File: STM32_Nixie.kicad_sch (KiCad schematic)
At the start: 0 parts

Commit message: added mcu symbol
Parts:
- added U?: STM32F100C4Tx, Package_QFP:LQFP-48_7x7mm_P0.5mm, symbol MCU_ST_STM32F1:STM32F100C4Tx
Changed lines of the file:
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@@
 (kicad_sch (version 20211123) (generator eeschema)
   (paper "A4")
+  (symbol (lib_id "MCU_ST_STM32F1:STM32F100C4Tx") (at 86.36 100.33 0) (unit 1)
+    (in_bom yes) (on_board yes) (fields_autoplaced)
+    (property "Reference" "U?" (id 0) (at 90.9194 138.43 0)
+      (effects (font (size 1.27 1.27)) (justify left))
+    )
+    (property "Value" "STM32F100C4Tx" (id 1) (at 90.9194 140.97 0)
+      (effects (font (size 1.27 1.27)) (justify left))
+    )
+    (property "Footprint" "Package_QFP:LQFP-48_7x7mm_P0.5mm" (id 2) (at 71.12 135.89 0)
+      (effects (font (size 1.27 1.27)) (justify right) hide)
+    )
+    (property "Datasheet" "http://www.st.com/st-web-ui/static/active/en/resource/technical/document/datasheet/CD00251732.pdf" (id 3) (at 86.36 100.33 0)
+      (effects (font (size 1.27 1.27)) hide)
+    )
+    (pin "1")
+    (pin "10")
+    (pin "11")
+    (pin "12")
+    (pin "13")
+    (pin "14")
+    (pin "15")
+    (pin "16")
+    (pin "17")
+    (pin "18")
+    (pin "19")
+    (pin "2")
+    (pin "20")
+    (pin "21")
+    (pin "22")
+    (pin "23")
+    (pin "24")
+    (pin "25")
+    (pin "26")
+    (pin "27")
+    (pin "28")
+    (pin "29")
+    (pin "3")
+    (pin "30")
+    (pin "31")
+    (pin "32")
+    (pin "33")
+    (pin "34")
+    (pin "35")
+    (pin "36")
+    (pin "37")
+    (pin "38")
+    (pin "39")
+    (pin "4")
+    (pin "40")
+    (pin "41")
+    (pin "42")
+    (pin "43")
+    (pin "44")
+    (pin "45")
+    (pin "46")
+    (pin "47")
+    (pin "48")
+    (pin "5")
+    (pin "6")
+    (pin "7")
+    (pin "8")
+    (pin "9")
+  )
   (sheet_instances
     (path "/" (page "1"))
   )
+  (symbol_instances
+    (path "/0270b2c5-4cd0-40ed-86dd-bdd60fed1e2d"
+      (reference "U?") (unit 1) (value "STM32F100C4Tx") (footprint "Package_QFP:LQFP-48_7x7mm_P0.5mm")
+    )
+  )
 )

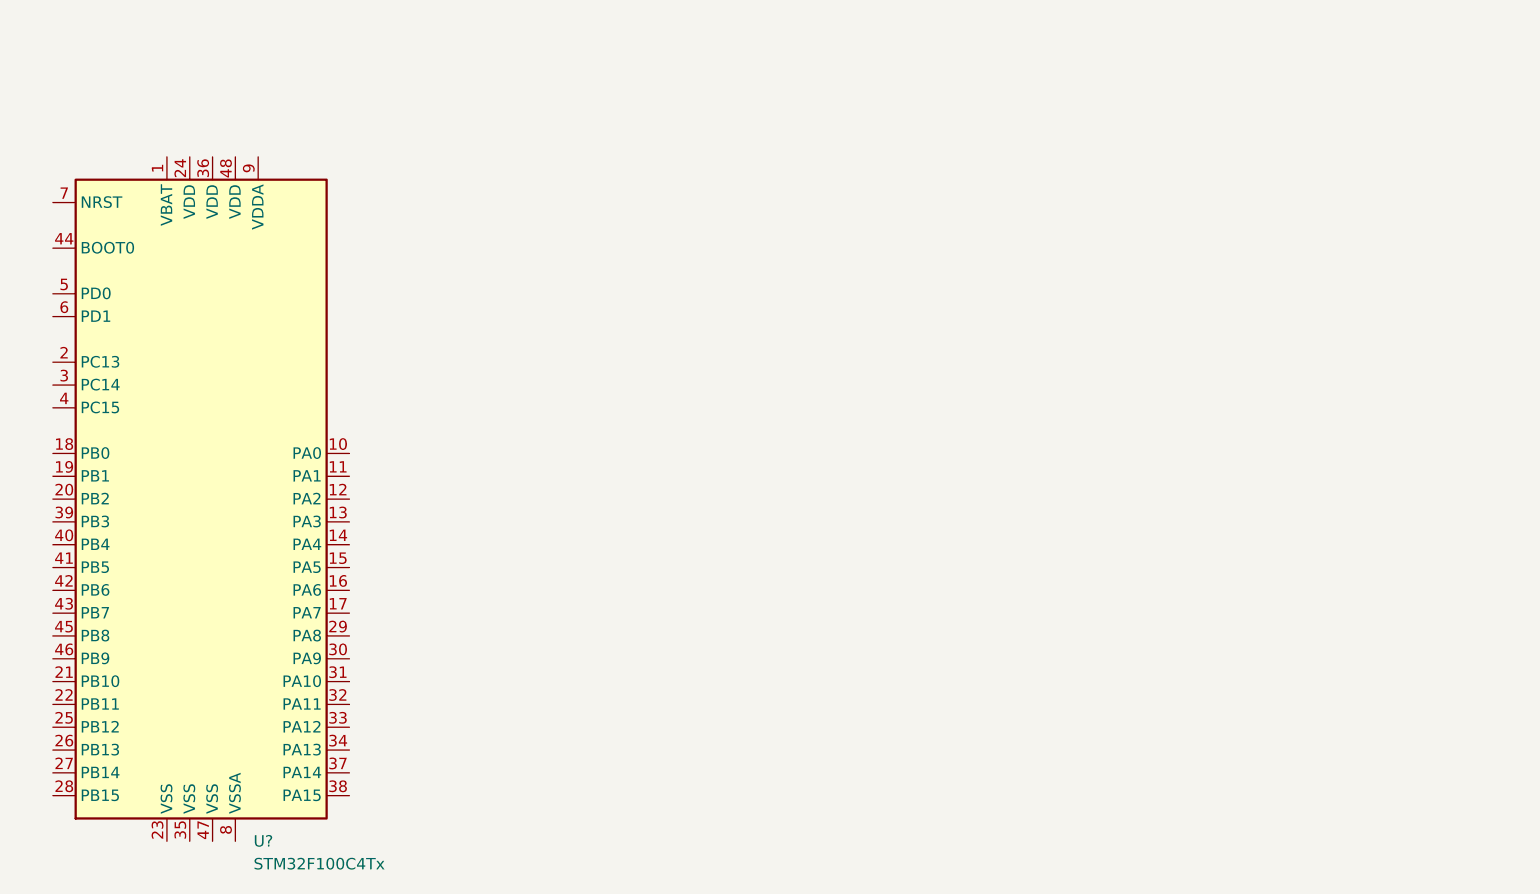
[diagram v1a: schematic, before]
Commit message: Added MCU page and shift register.
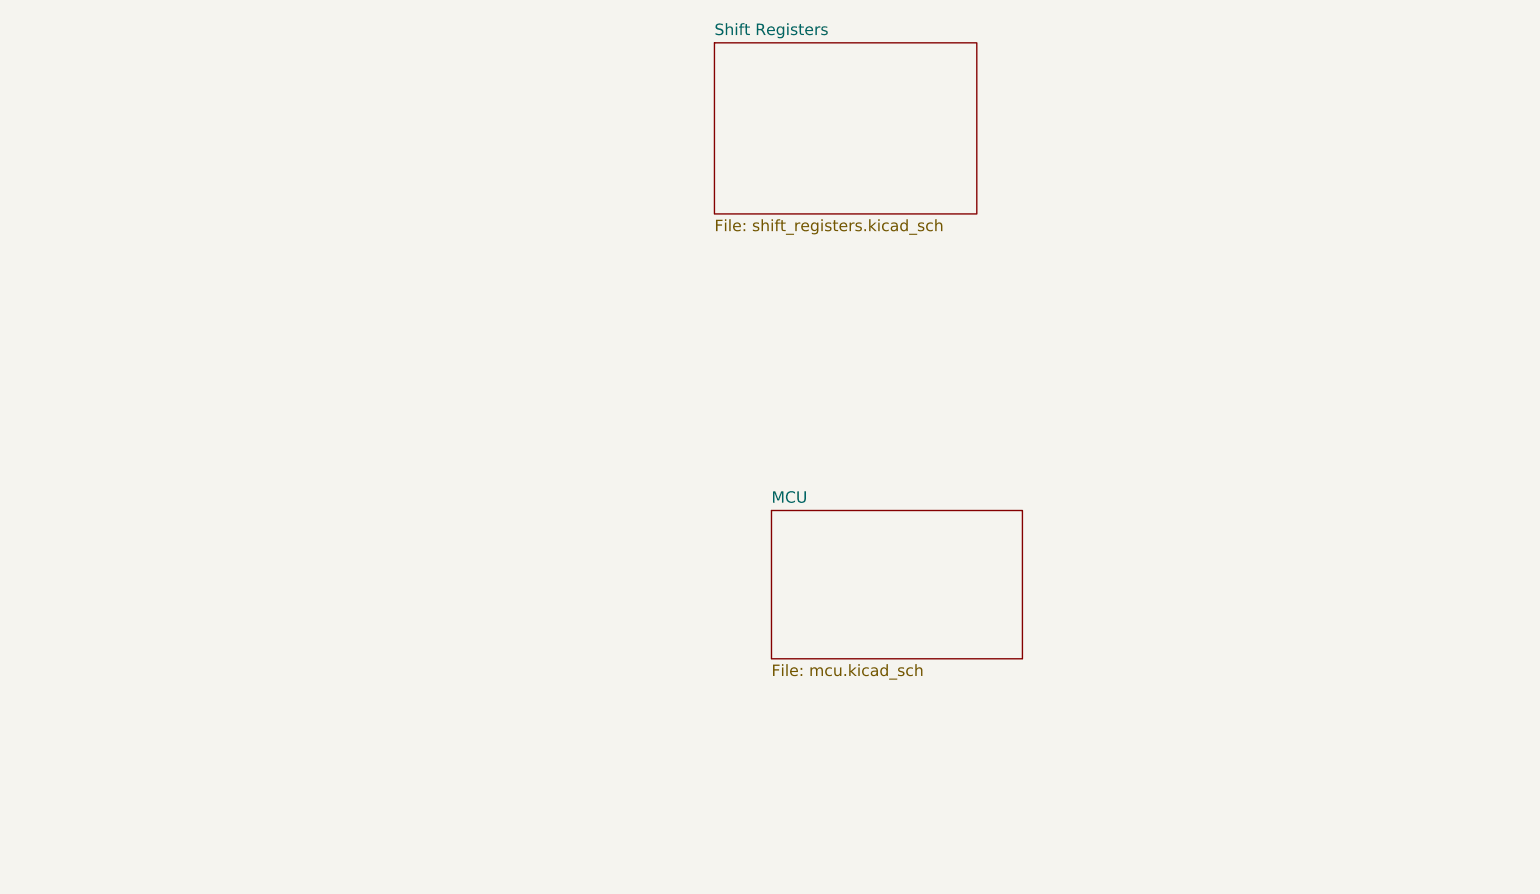
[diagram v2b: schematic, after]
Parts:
- removed U?: STM32F100C4Tx, Package_QFP:LQFP-48_7x7mm_P0.5mm, symbol MCU_ST_STM32F1:STM32F100C4Tx
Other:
- added sheet MCU (mcu.kicad_sch)
- added sheet Shift Registers (shift_registers.kicad_sch)
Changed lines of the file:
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@@
 (kicad_sch (version 20211123) (generator eeschema)
   (paper "A4")
-  (symbol (lib_id "MCU_ST_STM32F1:STM32F100C4Tx") (at 86.36 100.33 0) (unit 1)
-    (in_bom yes) (on_board yes) (fields_autoplaced)
-    (property "Reference" "U?" (id 0) (at 90.9194 138.43 0)
-      (effects (font (size 1.27 1.27)) (justify left))
+  (sheet (at 148.59 101.6) (size 27.94 16.51) (fields_autoplaced)
+    (stroke (width 0.1524) (type solid) (color 0 0 0 0))
+    (fill (color 0 0 0 0.0000))
+    (property "Sheet name" "MCU" (id 0) (at 148.59 100.8884 0)
+      (effects (font (size 1.27 1.27)) (justify left bottom))
     )
-    (property "Value" "STM32F100C4Tx" (id 1) (at 90.9194 140.97 0)
-      (effects (font (size 1.27 1.27)) (justify left))
+    (property "Sheet file" "mcu.kicad_sch" (id 1) (at 148.59 118.6946 0)
+      (effects (font (size 1.27 1.27)) (justify left top))
     )
-    (property "Footprint" "Package_QFP:LQFP-48_7x7mm_P0.5mm" (id 2) (at 71.12 135.89 0)
-      (effects (font (size 1.27 1.27)) (justify right) hide)
+  )
+  (sheet (at 142.24 49.53) (size 29.21 19.05) (fields_autoplaced)
+    (stroke (width 0.1524) (type solid) (color 0 0 0 0))
+    (fill (color 0 0 0 0.0000))
+    (property "Sheet name" "Shift Registers" (id 0) (at 142.24 48.8184 0)
+      (effects (font (size 1.27 1.27)) (justify left bottom))
     )
-    (property "Datasheet" "http://www.st.com/st-web-ui/static/active/en/resource/technical/document/datasheet/CD00251732.pdf" (id 3) (at 86.36 100.33 0)
-      (effects (font (size 1.27 1.27)) hide)
+    (property "Sheet file" "shift_registers.kicad_sch" (id 1) (at 142.24 69.1646 0)
+      (effects (font (size 1.27 1.27)) (justify left top))
     )
-    (pin "1")
-    (pin "10")
-    (pin "11")
-    (pin "12")
-    (pin "13")
-    (pin "14")
-    (pin "15")
-    (pin "16")
-    (pin "17")
-    (pin "18")
-    (pin "19")
-    (pin "2")
-    (pin "20")
-    (pin "21")
-    (pin "22")
-    (pin "23")
-    (pin "24")
-    (pin "25")
-    (pin "26")
-    (pin "27")
-    (pin "28")
-    (pin "29")
-    (pin "3")
-    (pin "30")
-    (pin "31")
-    (pin "32")
-    (pin "33")
-    (pin "34")
-    (pin "35")
-    (pin "36")
-    (pin "37")
-    (pin "38")
-    (pin "39")
-    (pin "4")
-    (pin "40")
-    (pin "41")
-    (pin "42")
-    (pin "43")
-    (pin "44")
-    (pin "45")
-    (pin "46")
-    (pin "47")
-    (pin "48")
-    (pin "5")
-    (pin "6")
-    (pin "7")
-    (pin "8")
-    (pin "9")
   )
   (sheet_instances
     (path "/" (page "1"))
+    (path "/f14ed119-44a4-4dba-a5a7-78813bb44ce1" (page "2"))
+    (path "/8ecdbb98-5b2a-4725-a227-62b58d0c66f3" (page "3"))
   )
   (symbol_instances
-    (path "/0270b2c5-4cd0-40ed-86dd-bdd60fed1e2d"
+    (path "/8ecdbb98-5b2a-4725-a227-62b58d0c66f3/53a1442c-3c5b-48fe-a89e-ea740fbbd2e1"
       (reference "U?") (unit 1) (value "STM32F100C4Tx") (footprint "Package_QFP:LQFP-48_7x7mm_P0.5mm")
     )
+    (path "/f14ed119-44a4-4dba-a5a7-78813bb44ce1/b3a9dbd4-2aab-41ed-8695-0bb972a07a2c"
+      (reference "U?") (unit 1) (value "IC_HV5622PG-G") (footprint "arjun_footprints:HV5622PG-G")
+    )
+    (path "/f14ed119-44a4-4dba-a5a7-78813bb44ce1/c5519631-1a61-407e-8a88-4a9f7dd4528e"
+      (reference "U?") (unit 1) (value "IC_HV5622PG-G") (footprint "arjun_footprints:HV5622PG-G")
+    )
   )

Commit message: added a nixie symbol
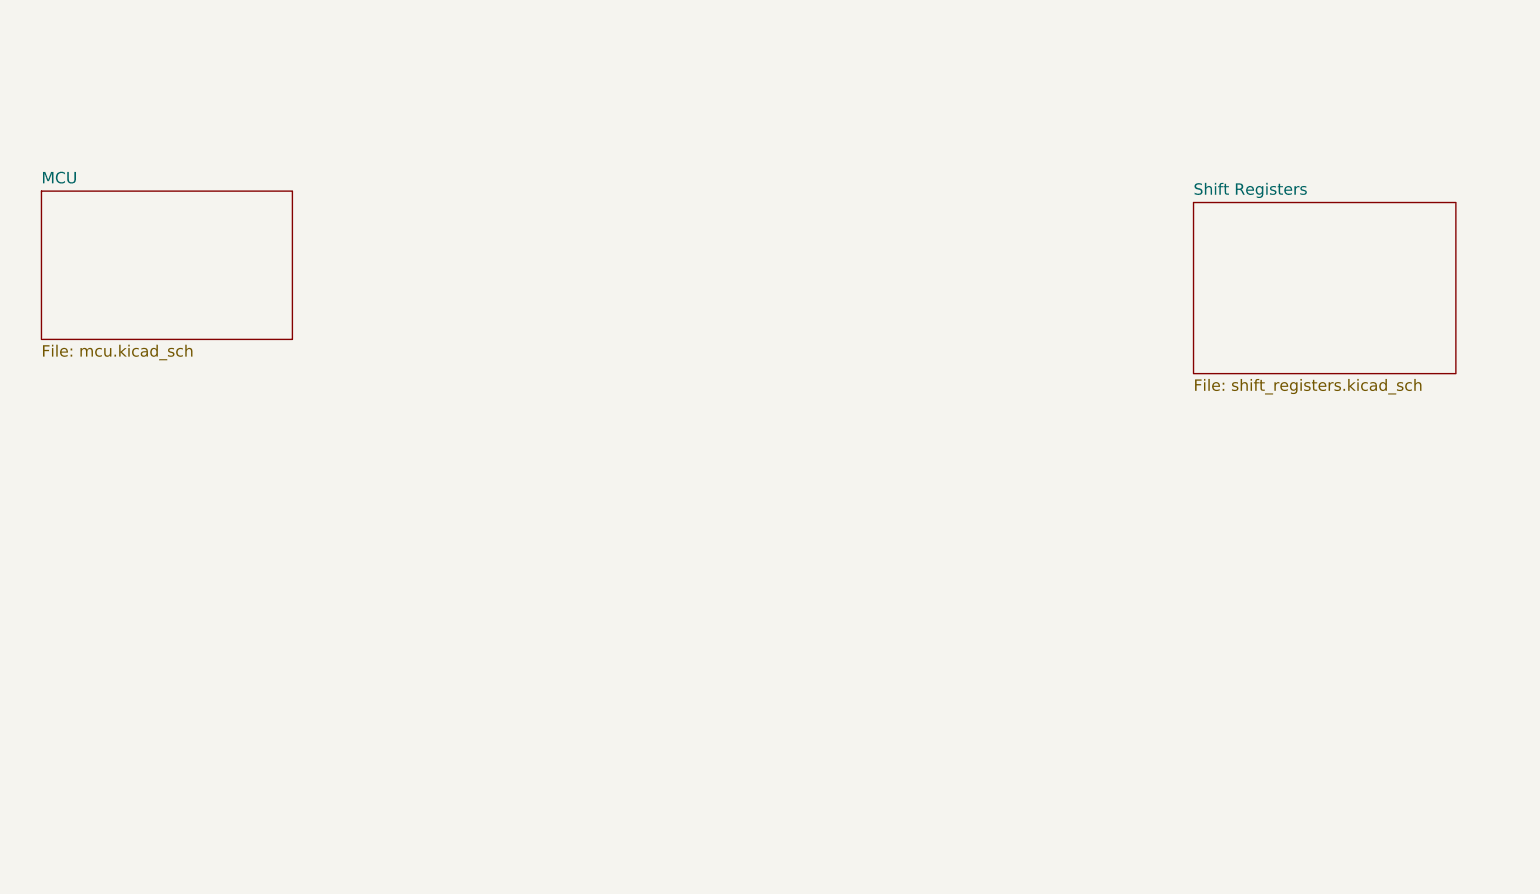
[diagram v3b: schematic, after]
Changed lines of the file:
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@@
 (kicad_sch (version 20211123) (generator eeschema)
   (paper "A4")
-  (sheet (at 148.59 101.6) (size 27.94 16.51) (fields_autoplaced)
+  (sheet (at 67.31 66.04) (size 27.94 16.51) (fields_autoplaced)
     (stroke (width 0.1524) (type solid) (color 0 0 0 0))
     (fill (color 0 0 0 0.0000))
-    (property "Sheet name" "MCU" (id 0) (at 148.59 100.8884 0)
+    (property "Sheet name" "MCU" (id 0) (at 67.31 65.3284 0)
       (effects (font (size 1.27 1.27)) (justify left bottom))
     )
-    (property "Sheet file" "mcu.kicad_sch" (id 1) (at 148.59 118.6946 0)
+    (property "Sheet file" "mcu.kicad_sch" (id 1) (at 67.31 83.1346 0)
       (effects (font (size 1.27 1.27)) (justify left top))
     )
   )
-  (sheet (at 142.24 49.53) (size 29.21 19.05) (fields_autoplaced)
+  (sheet (at 195.58 67.31) (size 29.21 19.05) (fields_autoplaced)
     (stroke (width 0.1524) (type solid) (color 0 0 0 0))
     (fill (color 0 0 0 0.0000))
-    (property "Sheet name" "Shift Registers" (id 0) (at 142.24 48.8184 0)
+    (property "Sheet name" "Shift Registers" (id 0) (at 195.58 66.5984 0)
       (effects (font (size 1.27 1.27)) (justify left bottom))
     )
-    (property "Sheet file" "shift_registers.kicad_sch" (id 1) (at 142.24 69.1646 0)
+    (property "Sheet file" "shift_registers.kicad_sch" (id 1) (at 195.58 86.9446 0)
       (effects (font (size 1.27 1.27)) (justify left top))
     )
@@
     (path "/f14ed119-44a4-4dba-a5a7-78813bb44ce1" (page "2"))
     (path "/8ecdbb98-5b2a-4725-a227-62b58d0c66f3" (page "3"))
+    (path "/f14ed119-44a4-4dba-a5a7-78813bb44ce1/47fb6452-bb5d-491d-bdc1-b44524035875" (page "4"))
   )
   (symbol_instances
+    (path "/f14ed119-44a4-4dba-a5a7-78813bb44ce1/47fb6452-bb5d-491d-bdc1-b44524035875/592da241-0f55-4f7a-a38f-5ee5a4570347"
+      (reference "N?") (unit 1) (value "IN-14") (footprint "arjun_footprints:IN-14")
+    )
+    (path "/f14ed119-44a4-4dba-a5a7-78813bb44ce1/47fb6452-bb5d-491d-bdc1-b44524035875/dfc4a792-6825-4000-958b-6cbb8aa83118"
+      (reference "R?") (unit 1) (value "R_US") (footprint "Resistor_SMD:R_1206_3216Metric_Pad1.30x1.75mm_HandSolder")
+    )
     (path "/8ecdbb98-5b2a-4725-a227-62b58d0c66f3/53a1442c-3c5b-48fe-a89e-ea740fbbd2e1"
       (reference "U?") (unit 1) (value "STM32F100C4Tx") (footprint "Package_QFP:LQFP-48_7x7mm_P0.5mm")

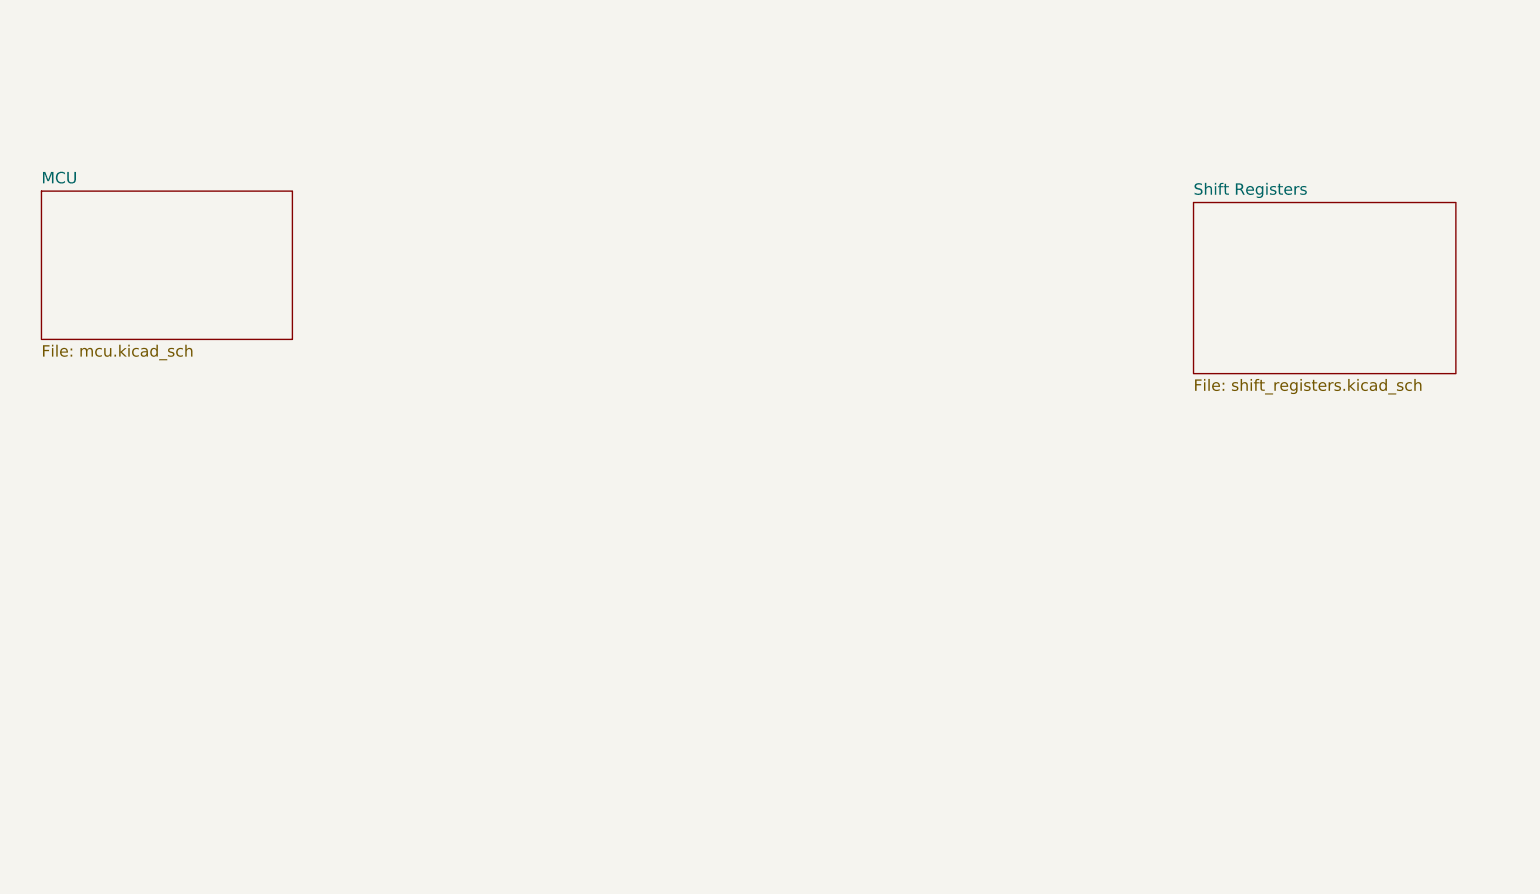
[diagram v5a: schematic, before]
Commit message: Added level shifter and finished up HV Shift Register page
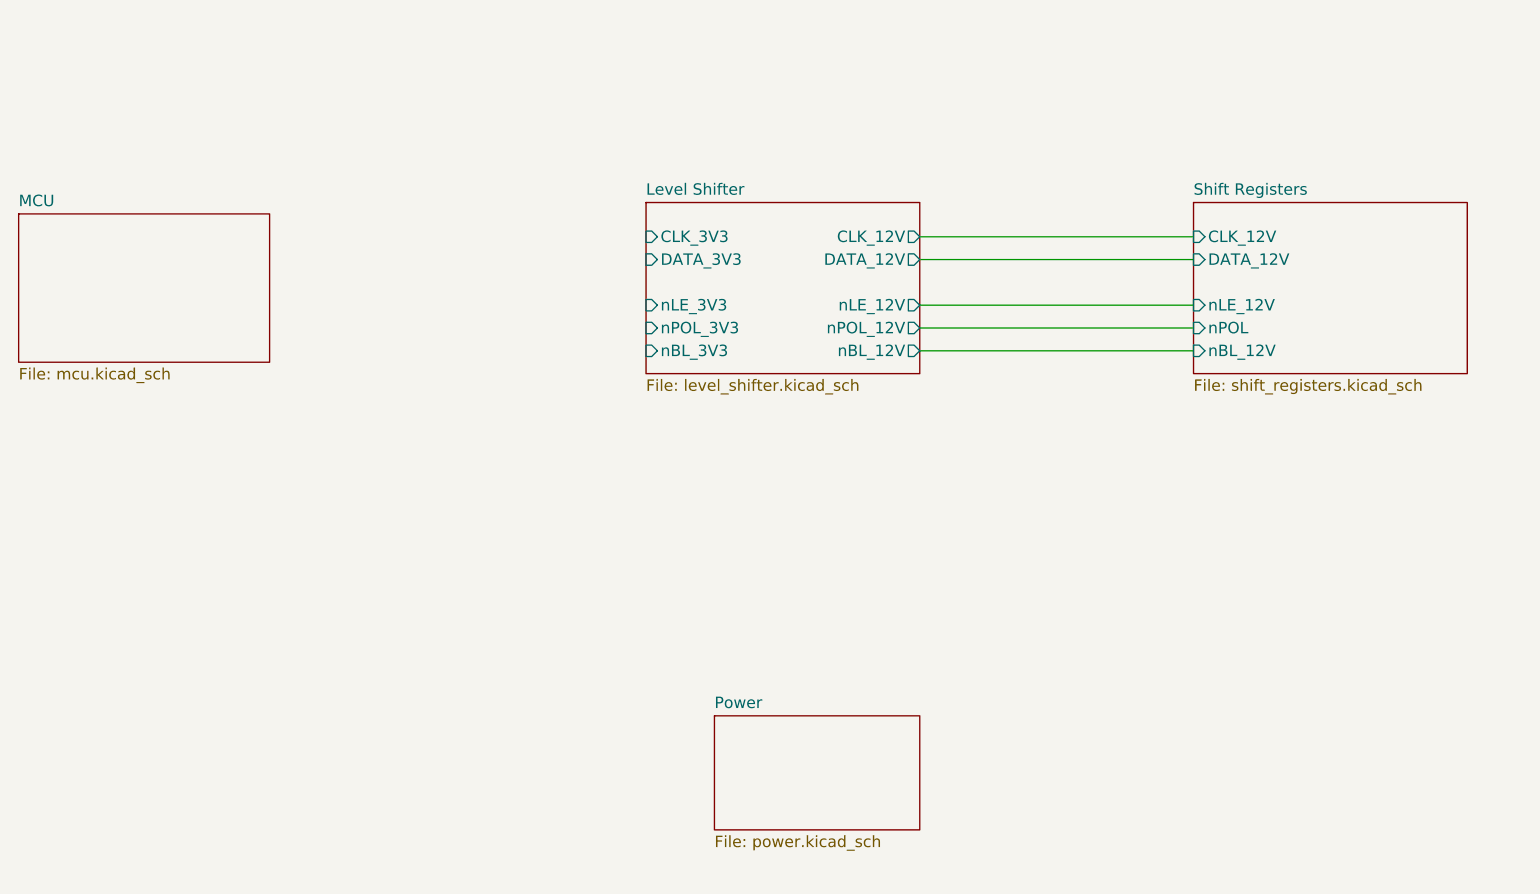
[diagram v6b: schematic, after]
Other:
- added sheet Level Shifter (level_shifter.kicad_sch)
- added sheet Power (power.kicad_sch)
- sheet Shift Registers ports: added CLK_12V, DATA_12V, nBL_12V, nLE_12V, nPOL; removed none
